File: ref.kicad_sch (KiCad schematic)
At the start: 41 parts, among them U6 REF7050, U61 OPA2189DGK, U62 OPA828DGN

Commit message: Adjust voltage rails.
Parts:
- R601, R602, R603, R61, R62, R63: footprint Resistor_SMD:R_1206_3216Metric -> Resistor_SMD:R_0603_1608Metric
- R604: renamed from R605; footprint Resistor_SMD:R_1206_3216Metric -> Resistor_SMD:R_0603_1608Metric
- R605: renamed from R607; footprint Resistor_SMD:R_1206_3216Metric -> Resistor_SMD:R_0603_1608Metric
- R606: renamed from R609; footprint Resistor_SMD:R_1206_3216Metric -> Resistor_SMD:R_0603_1608Metric
- renumbered R610 to R607
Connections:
- net +18V renamed +19V
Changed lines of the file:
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@@
 	(text "1⅔kΩ"
 		(exclude_from_sim no)
-		(at 172.72 99.06 0)
+		(at 172.72 99.314 0)
 		(effects
 			(font
@@
 			)
 		)
-		(property "Footprint" "Resistor_SMD:R_1206_3216Metric"
+		(property "Footprint" "Resistor_SMD:R_0603_1608Metric"
 			(at 162.56 73.152 90)
 			(effects
@@
 		(on_board yes)
 		(dnp no)
-		(property "Reference" "R607"
+		(property "Reference" "R605"
 			(at 168.402 101.6 90)
 			(effects
@@
 			)
 		)
-		(property "Footprint" "Resistor_SMD:R_1206_3216Metric"
+		(property "Footprint" "Resistor_SMD:R_0603_1608Metric"
 			(at 164.592 101.6 90)
 			(effects
@@
 			(project "lincal"
 				(path "/b054cef4-39e3-49d8-aff0-7ba5a206c187/525413b8-c4e9-4b1d-b0c6-ca0be2e26a7f"
-					(reference "R607")
+					(reference "R605")
 					(unit 1)
 				)
@@
 			)
 		)
-		(property "Footprint" "Resistor_SMD:R_1206_3216Metric"
+		(property "Footprint" "Resistor_SMD:R_0603_1608Metric"
 			(at 162.56 78.232 90)
 			(effects
@@
 			)
 		)
-		(property "Footprint" "Resistor_SMD:R_1206_3216Metric"
+		(property "Footprint" "Resistor_SMD:R_0603_1608Metric"
 			(at 162.56 68.072 90)
 			(effects
@@
 	)
 	(symbol
-		(lib_id "Parts:+18V")
+		(lib_id "Parts:+19V")
 		(at 96.52 82.55 0)
 		(unit 1)
@@
 		(on_board yes)
 		(dnp no)
-		(property "Reference" "#PWR0307"
+		(property "Reference" "#PWR307"
 			(at 96.52 86.36 0)
 			(effects
@@
 			)
 		)
-		(property "Value" "+18V"
+		(property "Value" "+19V"
 			(at 96.52 78.994 0)
 			(do_not_autoplace yes)
@@
 			)
 		)
-		(property "Description" "Power symbol creates a global label with name {dblquote}+18V{dblquote}"
+		(property "Description" "Power symbol creates a global label with name \"+19\""
 			(at 96.52 82.55 0)
 			(effects
@@
 			(project "lincal"
 				(path "/b054cef4-39e3-49d8-aff0-7ba5a206c187/525413b8-c4e9-4b1d-b0c6-ca0be2e26a7f"
-					(reference "#PWR0307")
+					(reference "#PWR307")
 					(unit 1)
 				)
@@
 	)
 	(symbol
-		(lib_id "Parts:+18V")
+		(lib_id "Parts:+19V")
 		(at 163.83 52.07 0)
 		(unit 1)
@@
 		(on_board yes)
 		(dnp no)
-		(property "Reference" "#PWR0115"
+		(property "Reference" "#PWR115"
 			(at 163.83 55.88 0)
 			(effects
@@
 			)
 		)
-		(property "Value" "+18V"
+		(property "Value" "+19V"
 			(at 163.83 48.514 0)
 			(do_not_autoplace yes)
@@
 			)
 		)
-		(property "Description" "Power symbol creates a global label with name {dblquote}+18V{dblquote}"
+		(property "Description" "Power symbol creates a global label with name \"+19\""
 			(at 163.83 52.07 0)
 			(effects
@@
 			(project "lincal"
 				(path "/b054cef4-39e3-49d8-aff0-7ba5a206c187/525413b8-c4e9-4b1d-b0c6-ca0be2e26a7f"
-					(reference "#PWR0115")
+					(reference "#PWR115")
 					(unit 1)
 				)
@@
 		(on_board yes)
 		(dnp no)
-		(property "Reference" "R609"
+		(property "Reference" "R606"
 			(at 168.402 111.76 90)
 			(effects
@@
 			)
 		)
-		(property "Footprint" "Resistor_SMD:R_1206_3216Metric"
+		(property "Footprint" "Resistor_SMD:R_0603_1608Metric"
 			(at 164.592 111.76 90)
 			(effects
@@
 			(project "lincal"
 				(path "/b054cef4-39e3-49d8-aff0-7ba5a206c187/525413b8-c4e9-4b1d-b0c6-ca0be2e26a7f"
-					(reference "R609")
+					(reference "R606")
 					(unit 1)
 				)
@@
 		(on_board yes)
 		(dnp no)
-		(property "Reference" "R610"
+		(property "Reference" "R607"
 			(at 168.402 121.92 90)
 			(effects
@@
 			(project "lincal"
 				(path "/b054cef4-39e3-49d8-aff0-7ba5a206c187/525413b8-c4e9-4b1d-b0c6-ca0be2e26a7f"
-					(reference "R610")
+					(reference "R607")
 					(unit 1)
 				)
@@
 		(on_board yes)
 		(dnp no)
-		(property "Reference" "R605"
+		(property "Reference" "R604"
 			(at 168.402 91.44 90)
 			(effects
@@
 			)
 		)
-		(property "Footprint" "Resistor_SMD:R_1206_3216Metric"
+		(property "Footprint" "Resistor_SMD:R_0603_1608Metric"
 			(at 164.592 91.44 90)
 			(effects
@@
 			(project "lincal"
 				(path "/b054cef4-39e3-49d8-aff0-7ba5a206c187/525413b8-c4e9-4b1d-b0c6-ca0be2e26a7f"
-					(reference "R605")
+					(reference "R604")
 					(unit 1)
 				)
@@
 			)
 		)
-		(property "Footprint" "Resistor_SMD:R_1206_3216Metric"
+		(property "Footprint" "Resistor_SMD:R_0603_1608Metric"
 			(at 136.652 59.69 90)
 			(effects
@@
 			)
 		)
-		(property "Footprint" "Resistor_SMD:R_1206_3216Metric"
+		(property "Footprint" "Resistor_SMD:R_0603_1608Metric"
 			(at 136.652 80.01 90)
 			(effects
@@
 			)
 		)
-		(property "Footprint" "Resistor_SMD:R_1206_3216Metric"
+		(property "Footprint" "Resistor_SMD:R_0603_1608Metric"
 			(at 136.652 69.85 90)
 			(effects

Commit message: Progress checkin.  About to redo FDA feedback again.
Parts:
- added C67, C71: 10n, Capacitor_SMD:C_0603_1608Metric, symbol Device:C
- added R70: 100, Resistor_SMD:R_0402_1005Metric, symbol Device:R
- R61, R62, R63: value 5k -> 4k99
- R611: footprint Resistor_SMD:R_0603_1608Metric -> Resistor_SMD:R_0402_1005Metric
- R66: value 1k5 -> 2k7; footprint Resistor_SMD:R_0402_1005Metric -> Resistor_SMD:R_0603_1608Metric; LCSC C25867 -> C13167
- R67: value 7k5 -> 33k; LCSC C23234 -> C4216
- R69: value 7k5 -> 7k15; LCSC C23234 -> (none); now left out of the parts list
- U62: footprint Parts:VSSOP-8-1EP_3x3mm_P0.65mm_EP1.57x1.89mm -> Parts:OPA828DGN
- renumbered C67 to C68, C68 to C69, C69 to C70
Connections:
- net GND: now also C67.2, C71.2
- net GNDPWR: no longer U61.5 (+)
- net Filt15: now reaches C6.1, R60.2, TP65.1, U62.3 (+)
- net at R61.2, R62.1: no longer U61.2 (-)
- net 10V: now reaches R602.2, R603.2
- net 10V: now also C67.1, R70.2
- net Ref10V: now reaches U61.6 (-), U61.7
- net at R62.2, R63.1: now also U61.2 (-)
- new net: C71.1, R70.1, U61.5 (+)
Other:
- moved on the sheet: R601, R602, R603, R611, U61B

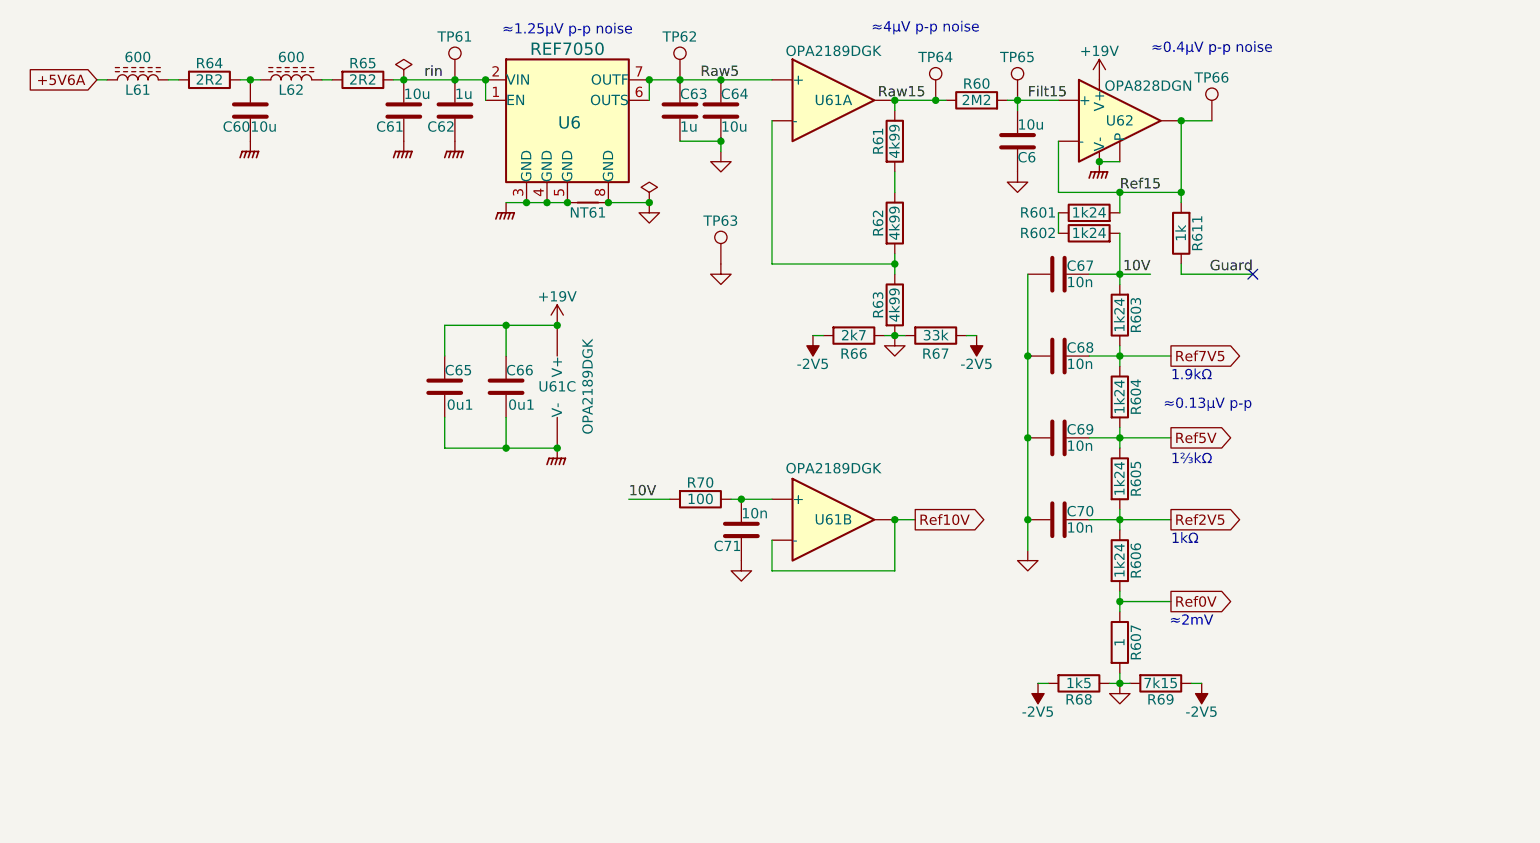
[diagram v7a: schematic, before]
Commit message: Start to place within physical board size.
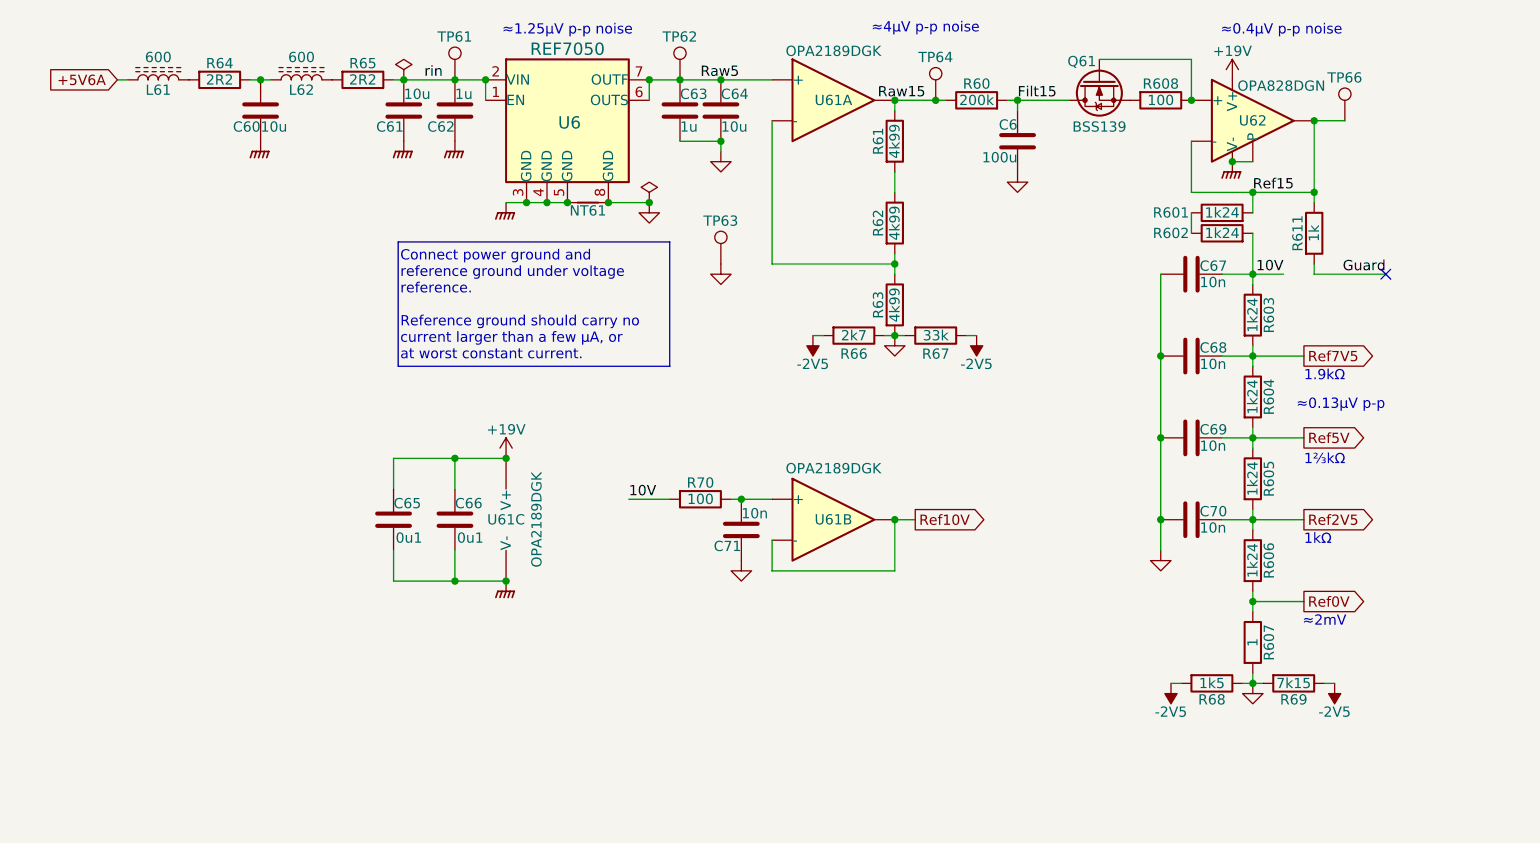
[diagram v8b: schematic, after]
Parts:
- removed TP65: TestPoint, Parts:TestPoint, symbol Connector:TestPoint
- added Q61: BSS139, Parts:SOT-23, symbol Parts:BSS139
- added R608: 100, Resistor_SMD:R_0402_1005Metric, symbol Device:R
- C6: value 10u -> 100u; footprint Parts:C_Rect_L31.5mm_W15.0mm_P27.50mm_MKS4 -> Parts:C_Big
- R60: value 2M2 -> 200k; LCSC C22938 -> (none)
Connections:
- net 10V: now also R603.1; no longer R603.2
- net Filt15: now also Q61.3 (D); no longer U62.3 (+)
- net Guard: now also R611.2; no longer R611.1
- net Ref15: now also R611.1; no longer R611.2
- net Ref7V5: now also R603.2; no longer R603.1
- new net: Q61.1 (G), R608.1, U62.3 (+)
- new net: Q61.2 (S), R608.2
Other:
- moved on the sheet: C60, C65, C66, C67, C68, C69, C70, L61, L62, R601, R602, R603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
